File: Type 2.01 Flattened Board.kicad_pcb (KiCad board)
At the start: 4 copper layers, 170 x 170 mm, 68 parts, among them J1 Conn_02x28_Odd_Even, J2 Conn_02x18_Odd_Even, J3 Conn_01x04, J4 Conn_02x03_Odd_Even, J5 Conn_02x03_Odd_Even, J6 Conn_02x28_Odd_Even, U1 74LVC1G79, U11 74AHC245, U13 74AHC04, U14 ATmega4809-PF, U16 ATmega4809-PF, U17 74AHC157, U18 74AHC573, U19 74AHC573, U2 74AHC245, U20 Adafruit_FeatherWing, U21 Adafruit_FeatherWing, U3 74AHC138, U4 74AHC245, U5 74AHC245, U6 74AHC245, U7 74LVC8T245, U8 74LVC8T245, U9 i960Sx_PLCC84

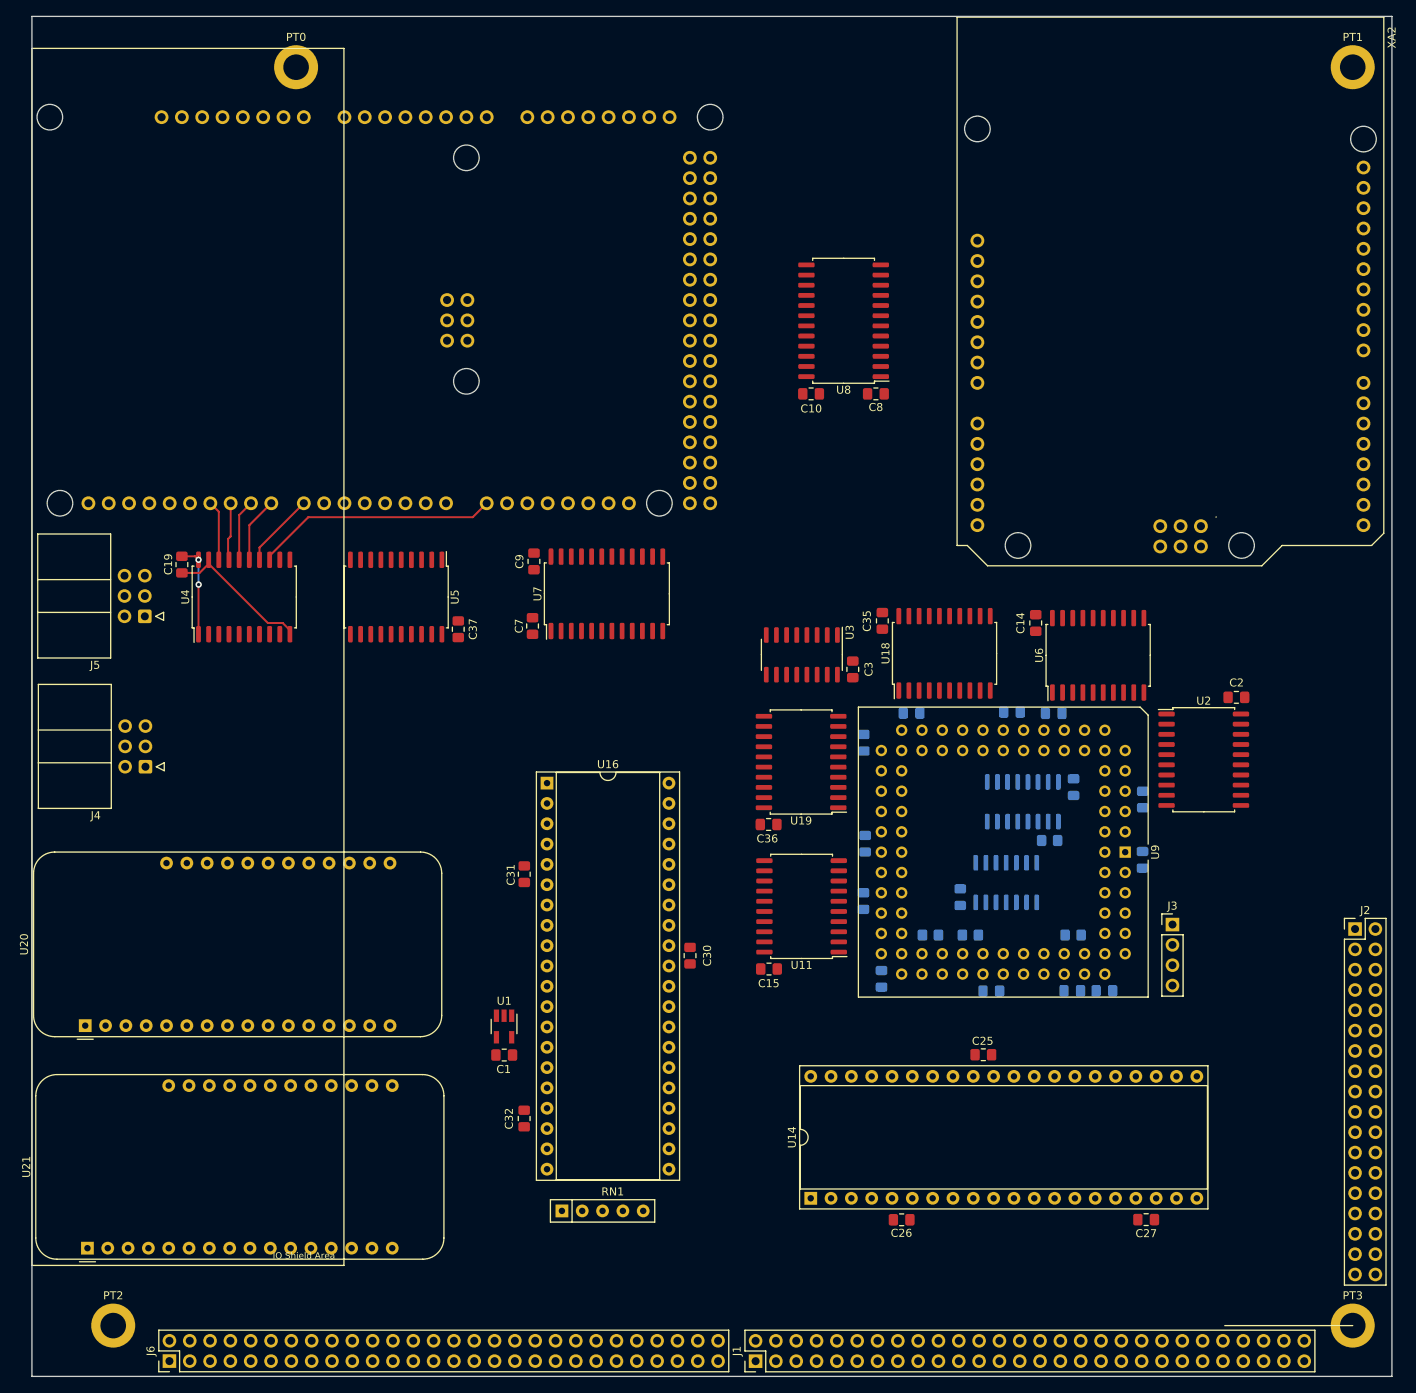
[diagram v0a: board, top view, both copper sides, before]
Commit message: Correct the feather symbol and breakouts
Also fix the VCC pin being bound to +5V for some reason. Use VCCIO
instead
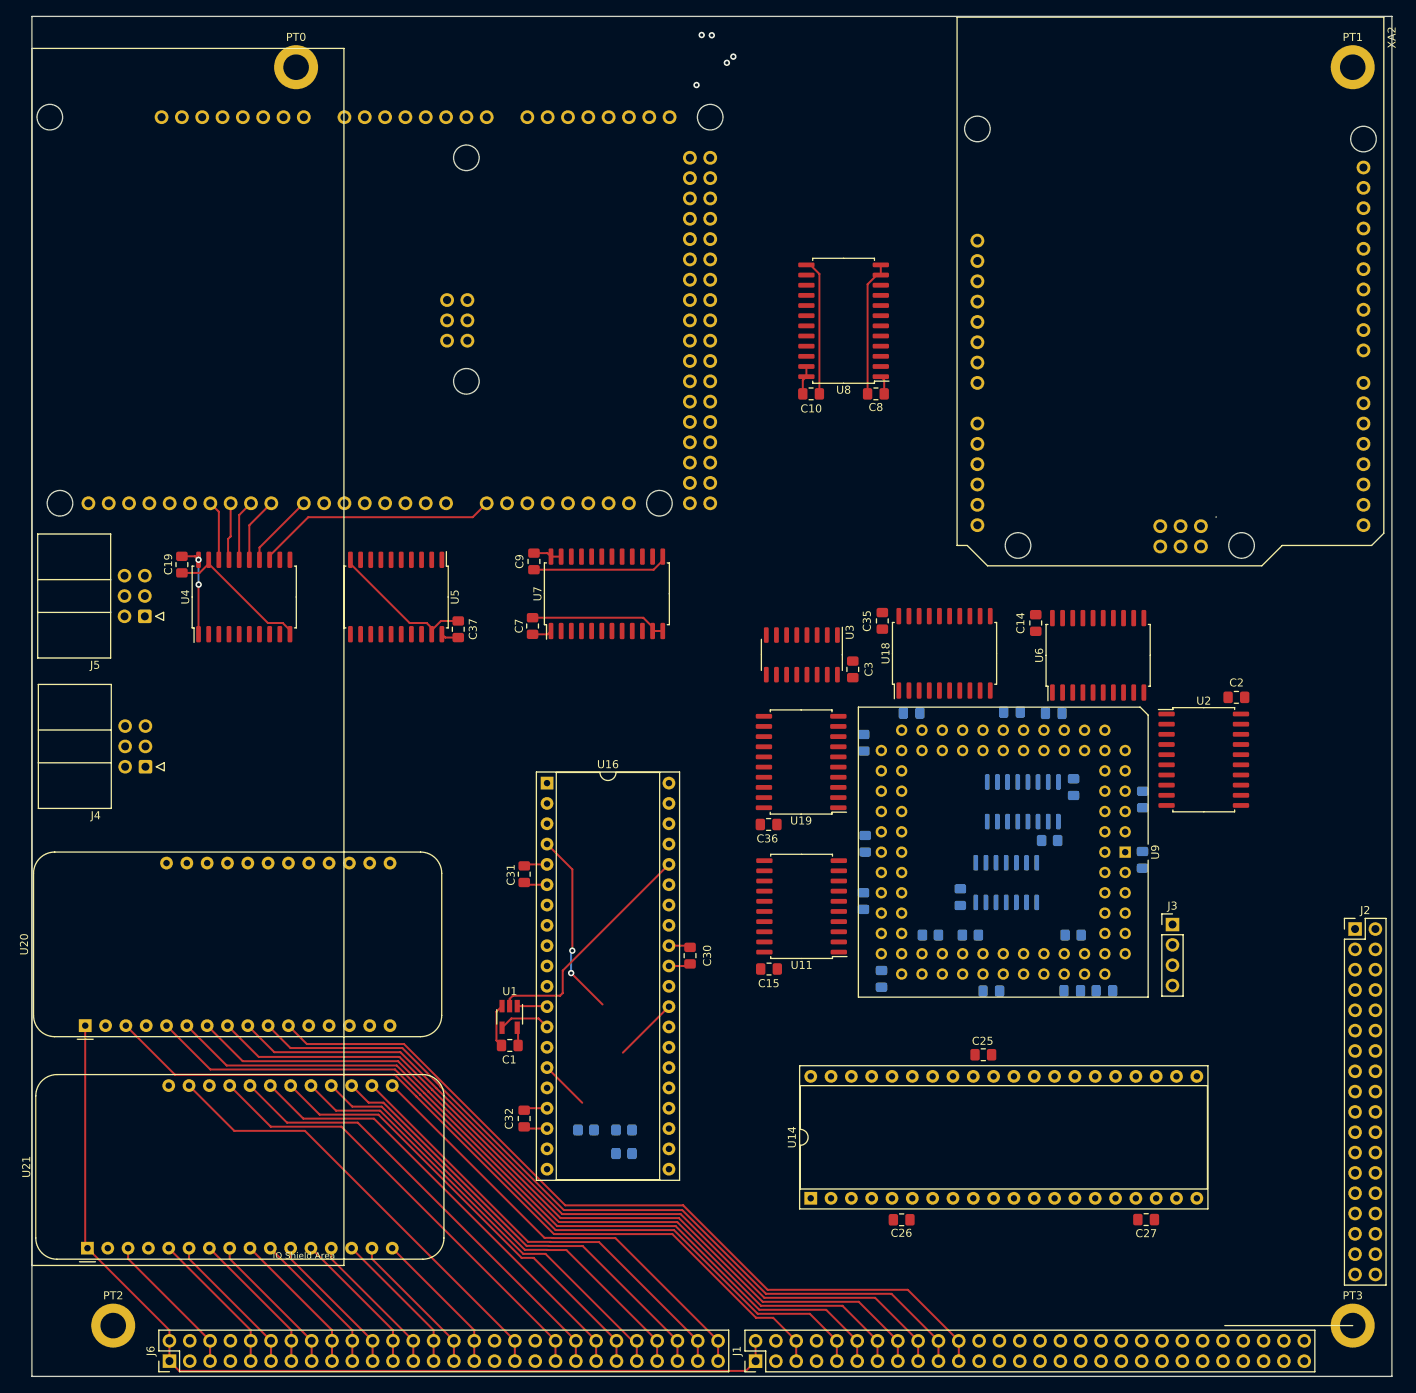
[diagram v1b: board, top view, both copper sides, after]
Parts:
- removed RN1: R_Network04, Resistor_THT:R_Array_SIP5
- added R5: 10k, Resistor_SMD:R_0805_2012Metric_Pad1.20x1.40mm_HandSolder, B.Cu at (69.3, 139.2)
- added R6: 10k, Resistor_SMD:R_0805_2012Metric_Pad1.20x1.40mm_HandSolder, B.Cu at (74.0, 142.1)
- added R7: 10k, Resistor_SMD:R_0805_2012Metric_Pad1.20x1.40mm_HandSolder, B.Cu at (74.0, 139.2)
- moved C1 1.39 mm to (59.7, 128.6)
- moved U1 1.39 mm to (59.7, 125.1)
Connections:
- C10 pad 1: +5V -> VCCB
- C14 pad 1: +5V -> VCCB
- C15 pad 1: +5V -> VCCB
- C19 pad 1: +5V -> VCCB
- C2 pad 1: +5V -> VCCB
- C3 pad 1: +5V -> VCCB
- C35 pad 1: +5V -> VCCB
- C36 pad 1: +5V -> VCCB
- C9 pad 1: +5V -> VCCB
- J1 pad 1: /Feather.FREE -> /~{RESET_{0}}
- J1 pad 10: /Feather.MOSI -> /Feather.A0
- J1 pad 11: /Feather.SCK -> /Feather.A1
- J1 pad 12: /Feather.SCK -> /Feather.A1
- J1 pad 13: /GCM4.~{FEATHER_INT0} -> /Feather.A2
- J1 pad 14: /GCM4.~{FEATHER_INT0} -> /Feather.A2
- J1 pad 15: /Feather.A4 -> /Feather.A3
- J1 pad 16: /Feather.A4 -> /Feather.A3
- J1 pad 17: /Feather.A3 -> /Feather.A4
- J1 pad 18: /Feather.A3 -> /Feather.A4
- J1 pad 19: /Feather.A2 -> /GCM4.~{FEATHER_INT0}
- J1 pad 2: /Feather.FREE -> /~{RESET_{0}}
- J1 pad 20: /Feather.A2 -> /GCM4.~{FEATHER_INT0}
- J1 pad 21: /Feather.A1 -> /Feather.SCK
- J1 pad 22: /Feather.A1 -> /Feather.SCK
- J1 pad 23: /Feather.A0 -> /Feather.MOSI
- J1 pad 24: /Feather.A0 -> /Feather.MOSI
- J1 pad 25: GND -> /Feather.MISO
- J1 pad 26: GND -> /Feather.MISO
- J1 pad 27: /Feather.AREF -> /UART1.TX
- J1 pad 28: /Feather.AREF -> /UART1.TX
- J1 pad 29: +3V3 -> /UART1.RX
- J1 pad 3: /UART1.RX -> +3V3
- J1 pad 30: +3V3 -> /UART1.RX
- J1 pad 31: /~{RESET_{0}} -> /Feather.FREE
- J1 pad 32: /~{RESET_{0}} -> /Feather.FREE
- J1 pad 4: /UART1.RX -> +3V3
- J1 pad 5: /UART1.TX -> /Feather.AREF
- J1 pad 6: /UART1.TX -> /Feather.AREF
- J1 pad 7: /Feather.MISO -> GND
- J1 pad 8: /Feather.MISO -> GND
- J1 pad 9: /Feather.MOSI -> /Feather.A0
- J6 pad 1: /Feather2.FREE -> /~{RESET_{0}}
- J6 pad 10: /Feather2.MOSI -> /Feather2.A0
- J6 pad 11: /Feather2.SCK -> /Feather2.A1
- J6 pad 12: /Feather2.SCK -> /Feather2.A1
- J6 pad 13: /GCM4.~{FEATHER_INT1} -> /Feather2.A2
- J6 pad 14: /GCM4.~{FEATHER_INT1} -> /Feather2.A2
- J6 pad 15: /Feather2.A4 -> /Feather2.A3
- J6 pad 16: /Feather2.A4 -> /Feather2.A3
- J6 pad 17: /Feather2.A3 -> /Feather2.A4
- J6 pad 18: /Feather2.A3 -> /Feather2.A4
- J6 pad 19: /Feather2.A2 -> /GCM4.~{FEATHER_INT1}
- J6 pad 2: /Feather2.FREE -> /~{RESET_{0}}
- J6 pad 20: /Feather2.A2 -> /GCM4.~{FEATHER_INT1}
- J6 pad 21: /Feather2.A1 -> /Feather2.SCK
- J6 pad 22: /Feather2.A1 -> /Feather2.SCK
- J6 pad 23: /Feather2.A0 -> /Feather2.MOSI
- J6 pad 24: /Feather2.A0 -> /Feather2.MOSI
- J6 pad 25: GND -> /Feather2.MISO
- J6 pad 26: GND -> /Feather2.MISO
- J6 pad 27: /Feather2.AREF -> /UART2.TX
- J6 pad 28: /Feather2.AREF -> /UART2.TX
- J6 pad 29: +3V3 -> /UART2.RX
- J6 pad 3: /UART2.RX -> +3V3
- J6 pad 30: +3V3 -> /UART2.RX
- J6 pad 31: /~{RESET_{0}} -> /Feather2.FREE
- J6 pad 32: /~{RESET_{0}} -> /Feather2.FREE
- J6 pad 4: /UART2.RX -> +3V3
- J6 pad 5: /UART2.TX -> /Feather2.AREF
- J6 pad 6: /UART2.TX -> /Feather2.AREF
- J6 pad 7: /Feather2.MISO -> GND
- J6 pad 8: /Feather2.MISO -> GND
- J6 pad 9: /Feather2.MOSI -> /Feather2.A0
- U11 pad 1: +5V -> VCCB
- U11 pad 20: +5V -> VCCB
- U18 pad 20: +5V -> VCCB
- U19 pad 20: +5V -> VCCB
- U2 pad 1: +5V -> VCCB
- U2 pad 20: +5V -> VCCB
- U20 pad 1: /Feather.FREE -> /~{RESET_{0}}
- U20 pad 10: /Feather.A2 -> /GCM4.~{FEATHER_INT0}
- U20 pad 11: /Feather.A1 -> /Feather.SCK
- U20 pad 12: /Feather.A0 -> /Feather.MOSI
- U20 pad 13: GND -> /Feather.MISO
- U20 pad 14: /Feather.AREF -> /UART1.TX
- U20 pad 15: +3V3 -> /UART1.RX
- U20 pad 16: /~{RESET_{0}} -> /Feather.FREE
- U20 pad 17: +3V3 -> /Feather.SDA
- U20 pad 18: /Feather.EN -> /Feather.SCL
- U20 pad 19: +5V -> /Feather.D5
- U20 pad 2: /UART1.RX -> +3V3
- U20 pad 20: /Feather.D13 -> /Feather.D6
- U20 pad 21: /Feather.D12 -> /Feather.D9
- U20 pad 22: /Feather.D11 -> /Feather.D10
- U20 pad 23: /Feather.D10 -> /Feather.D11
- U20 pad 24: /Feather.D9 -> /Feather.D12
- U20 pad 25: /Feather.D6 -> /Feather.D13
- U20 pad 26: /Feather.D5 -> +5V
- U20 pad 27: /Feather.SCL -> /Feather.EN
- U20 pad 28: /Feather.SDA -> +3V3
- U20 pad 3: /UART1.TX -> /Feather.AREF
- U20 pad 4: /Feather.MISO -> GND
- U20 pad 5: /Feather.MOSI -> /Feather.A0
- U20 pad 6: /Feather.SCK -> /Feather.A1
- U20 pad 7: /GCM4.~{FEATHER_INT0} -> /Feather.A2
- U20 pad 8: /Feather.A4 -> /Feather.A3
- U20 pad 9: /Feather.A3 -> /Feather.A4
- U21 pad 1: /Feather2.FREE -> /~{RESET_{0}}
- U21 pad 10: /Feather2.A2 -> /GCM4.~{FEATHER_INT1}
- U21 pad 11: /Feather2.A1 -> /Feather2.SCK
- U21 pad 12: /Feather2.A0 -> /Feather2.MOSI
- U21 pad 13: GND -> /Feather2.MISO
- U21 pad 14: /Feather2.AREF -> /UART2.TX
- U21 pad 15: +3V3 -> /UART2.RX
- U21 pad 16: /~{RESET_{0}} -> /Feather2.FREE
- U21 pad 17: +3V3 -> /Feather2.SDA
- U21 pad 18: /Feather2.EN -> /Feather2.SCL
- U21 pad 19: +5V -> /Feather2.D5
- U21 pad 2: /UART2.RX -> +3V3
- U21 pad 20: /Feather2.D13 -> /Feather2.D6
- U21 pad 21: /Feather2.D12 -> /Feather2.D9
- U21 pad 22: /Feather2.D11 -> /Feather2.D10
- U21 pad 23: /Feather2.D10 -> /Feather2.D11
- U21 pad 24: /Feather2.D9 -> /Feather2.D12
- U21 pad 25: /Feather2.D6 -> /Feather2.D13
- U21 pad 26: /Feather2.D5 -> +5V
- U21 pad 27: /Feather2.SCL -> /Feather2.EN
- U21 pad 28: /Feather2.SDA -> +3V3
- U21 pad 3: /UART2.TX -> /Feather2.AREF
- U21 pad 4: /Feather2.MISO -> GND
- U21 pad 5: /Feather2.MOSI -> /Feather2.A0
- U21 pad 6: /Feather2.SCK -> /Feather2.A1
- U21 pad 7: /GCM4.~{FEATHER_INT1} -> /Feather2.A2
- U21 pad 8: /Feather2.A4 -> /Feather2.A3
- U21 pad 9: /Feather2.A3 -> /Feather2.A4
- U3 pad 16: +5V -> VCCB
- U3 pad 6: +5V -> VCCB
- U4 pad 1: +5V -> VCCB
- U4 pad 20: +5V -> VCCB
- U6 pad 1: +5V -> VCCB
- U6 pad 20: +5V -> VCCB
- U7 pad 23: +5V -> VCCB
- U7 pad 24: +5V -> VCCB
- U8 pad 23: +5V -> VCCB
- U8 pad 24: +5V -> VCCB
- XA1 pad IORF: +5V -> VCCB
- XA2 pad IORF: +5V -> VCCB
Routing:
- net /~{RESET_{0}}: track 0.00 -> 257.8 mm, vias 0 -> 2
- net /Feather.D12: track 0.00 -> 151.7 mm
- net /Feather.D13: track 0.00 -> 151.6 mm
- net /Feather.EN: track 0.00 -> 151.6 mm
- net /VIN: track 0.00 -> 133.6 mm, vias 0 -> 2
- net /MOSI: track 0.00 -> 126.9 mm
- net /MISO: track 0.00 -> 124.4 mm
- net /SCK: track 0.00 -> 120.0 mm
- net /Feather.FREE: track 0.00 -> 112.1 mm
- net /~{CS}: track 0.00 -> 111.7 mm, vias 0 -> 1
- net /UART1.RX: track 0.00 -> 111.1 mm
- net /UART1.TX: track 0.00 -> 110.9 mm
- net /Feather.MISO: track 0.00 -> 110.9 mm
- net /Feather.MOSI: track 0.00 -> 110.6 mm
- net /GCM4.~{FEATHER_INT0}: track 0.00 -> 102.7 mm
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
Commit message: More lines being routed. Looks pretty clean so far
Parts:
- moved J4 141.8 mm to (155.9, 98.4), turned to 0 degrees
- moved R6 39.0 mm to (69.1, 103.5), turned to 0 degrees
- moved R7 15.5 mm to (75.9, 123.8)
- moved R5 7.91 mm to (67.9, 131.4), turned to 0 degrees
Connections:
- U11 pad 3: /i960.BURST_A1 -> /i960.~{BE0}
- U11 pad 4: /i960.BURST_A2 -> /i960.~{BE1}
- U11 pad 5: /i960.BURST_A3 -> /i960.BURST_A1
- U11 pad 6: /i960.~{BE0} -> /i960.BURST_A2
- U11 pad 7: /i960.~{BE1} -> /i960.BURST_A3
- U19 pad 1: /i960/GCM4.~{DEV_EN0} -> /i960/i960.~{DEV_EN0}
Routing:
- net GND: track 120.1 -> 313.1 mm
- net /Feather.SDA: track 0.00 -> 161.3 mm
- net /Feather.SCL: track 0.00 -> 160.4 mm
- net /Feather.D5: track 0.00 -> 159.4 mm
- net /Feather.D6: track 0.00 -> 158.3 mm
- net /Feather.D9: track 0.00 -> 157.2 mm
- net /Feather.D10: track 0.00 -> 156.2 mm
- net /Feather.D11: track 0.00 -> 155.1 mm
- net +5V: track 17.9 -> 81.9 mm
- net /i960/PIC.PD0: track 0.00 -> 57.8 mm
- net Net-(U16-Pad26): track 0.00 -> 54.4 mm, vias 0 -> 1
- net /i960/PIC.PD1: track 0.00 -> 54.1 mm
- net /GCM4.L5: track 0.00 -> 51.3 mm, vias 0 -> 1
- net /GCM4.L3: track 0.00 -> 51.2 mm, vias 0 -> 1
- net /i960/PIC.PD2: track 0.00 -> 50.3 mm
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
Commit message: More layout fixes and bug fixes
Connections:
- U3 pad 4: /i960/GCM4.~{EN} -> /GCM4.~{EN}
- XA1 pad D23: /BUS.PA15 -> /GCM4.~{EN}
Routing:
- net /i960.D1: track 0.00 -> 50.5 mm, vias 0 -> 2
- net /i960.D0: track 0.00 -> 49.2 mm, vias 0 -> 1
- net /i960.D2: track 7.15 -> 46.1 mm, vias 0 -> 2
- net /i960.W\~{R}: track 0.00 -> 38.9 mm, vias 0 -> 2
- net /i960/i960.~{DEV_EN4}: track 0.00 -> 38.2 mm
- net /i960.D3: track 10.2 -> 47.6 mm, vias 0 -> 2
- net /i960.D4: track 7.15 -> 43.0 mm, vias 0 -> 2
- net /i960.D5: track 10.1 -> 44.3 mm, vias 0 -> 2
- net /i960.D6: track 7.15 -> 39.8 mm, vias 0 -> 2
- net /i960.D7: track 11.2 -> 42.1 mm, vias 0 -> 2
- net /GCM4.~{EN}: track 0.00 -> 27.9 mm
- net /i960/i960.~{DEV_EN1}: track 11.3 -> 0.45 mm
- net /i960/K3: track 0.00 -> 6.80 mm
- net /i960/K0: track 0.00 -> 6.27 mm
- net /GCM4.L7: vias 1 -> 2
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
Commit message: More routing operations
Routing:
- net /GCM4.L7: track 49.0 -> 147.8 mm, vias 2 -> 4
- net /GCM4.L6: track 46.2 -> 110.0 mm, vias 2 -> 3
- net /GCM4.L5: track 51.3 -> 114.4 mm, vias 2 -> 3
- net /GCM4.L4: track 46.1 -> 108.5 mm, vias 2 -> 3
- net /GCM4.L3: track 51.2 -> 113.5 mm, vias 2 -> 3
- net /GCM4.L2: track 46.3 -> 107.9 mm, vias 2 -> 3
- net /GCM4.L1: track 49.8 -> 111.4 mm, vias 1 -> 2
- net /GCM4.L0: track 44.7 -> 104.2 mm, vias 1 -> 2
- net /i960.D0: track 49.2 -> 0.00 mm
- net /i960.D1: track 50.5 -> 10.1 mm
- net /i960.D2: track 46.1 -> 7.15 mm
- net /i960/i960.~{DEV_EN4}: track 38.2 -> 0.00 mm
- net /i960.D3: track 47.6 -> 10.2 mm
- net /i960.D4: track 43.0 -> 7.15 mm
- net /i960.D5: track 44.3 -> 10.1 mm
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
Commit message: More layout changes
Most importantly, move the ~{AS} and CLK,CLK2 pins to separate breakout
headers
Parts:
- added J7: Conn_01x02, Connector_PinHeader_2.54mm:PinHeader_1x02_P2.54mm_Vertical, F.Cu at (110.6, 128.3)
- J3: value Conn_01x04 -> Conn_01x01; footprint Connector_PinHeader_2.54mm:PinHeader_1x04_P2.54mm_Vertical -> Connector_PinHeader_2.54mm:PinHeader_1x01_P2.54mm_Vertical
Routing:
- net /i960.DT\~{R}: track 0.00 -> 90.0 mm, vias 0 -> 4
- net /i960/PIC.PA6: track 0.00 -> 88.6 mm
- net /i960/PIC.PC0: track 0.00 -> 88.0 mm
- net /i960/PIC.PC1: track 0.00 -> 82.8 mm
- net /i960/PIC.PC2: track 0.00 -> 78.1 mm
- net /i960/UPDI_RXD2: track 0.00 -> 72.3 mm
- net /GCM4.D0: track 0.00 -> 69.4 mm
- net /i960/UPDI_TXD2: track 0.00 -> 69.2 mm
- net /GCM4.D1: track 0.00 -> 66.6 mm
- net /GCM4.D2: track 0.00 -> 64.4 mm
- net /GCM4.D3: track 0.00 -> 62.9 mm
- net /GCM4.L5: track 114.4 -> 175.9 mm, vias 3 -> 4
- net /GCM4.L6: track 110.0 -> 169.4 mm, vias 3 -> 4
- net /GCM4.L4: track 108.5 -> 167.7 mm, vias 3 -> 4
- net /GCM4.L2: track 107.9 -> 166.7 mm, vias 3 -> 4
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
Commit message: More trace layouts
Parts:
- added J10: Conn_01x02, Connector_PinHeader_2.54mm:PinHeader_1x02_P2.54mm_Vertical, F.Cu at (84.1, 136.5)
- added J8: Conn_01x01, Connector_PinHeader_2.54mm:PinHeader_1x01_P2.54mm_Vertical, F.Cu at (59.6, 100.9)
- added J9: Conn_01x01, Connector_PinHeader_2.54mm:PinHeader_1x01_P2.54mm_Vertical, F.Cu at (56.1, 133.9)
- J7: value Conn_01x02 -> Conn_01x08; footprint Connector_PinHeader_2.54mm:PinHeader_1x02_P2.54mm_Vertical -> Connector_PinHeader_2.54mm:PinHeader_1x08_P2.54mm_Vertical
- moved J7 61.7 mm to (61.8, 90.5)
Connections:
- J7 pad 1: /i960.CLK -> /i960/ME.PA0
- J7 pad 2: /i960.CLK2 -> /i960/ME.PA1
- U16 pad 10: /i960.~{BE1} -> /i960.~{BE0}
- U16 pad 9: /i960.~{BE0} -> /i960.~{BE1}
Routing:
- net /BUS.PB14: track 0.00 -> 141.9 mm, vias 0 -> 3
- net /BUS.PB15: track 0.00 -> 141.9 mm, vias 0 -> 3
- net /i960/i960.~{BLAST}: track 0.00 -> 74.8 mm, vias 0 -> 1
- net /i960/UPDI_RXD: track 0.00 -> 69.9 mm
- net /i960/UPDI_TXD: track 0.00 -> 67.3 mm
- net /i960/5V_~{RESET}: track 2.72 -> 54.6 mm, vias 0 -> 1
- net /i960.~{BE0}: track 8.89 -> 47.1 mm, vias 0 -> 1
- net /i960.~{BE1}: track 5.93 -> 43.6 mm, vias 0 -> 1
- net /i960/ME.PA0: track 0.00 -> 31.4 mm, vias 0 -> 1
- net /i960/ME.PA1: track 0.00 -> 28.0 mm, vias 0 -> 1
- net /i960/ME.PA2: track 0.00 -> 24.6 mm, vias 0 -> 1
- net /i960/ME.PA4: track 0.00 -> 16.1 mm
- net /i960.CLK: track 79.5 -> 92.7 mm
- net /i960/ME.PA5: track 0.00 -> 12.5 mm
- net /~{CS}: track 111.7 -> 123.0 mm
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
